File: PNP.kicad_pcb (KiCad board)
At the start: 4 copper layers, 98.3 x 100 mm, 41 parts, among them J1 Conn_01x04_Socket, J10 Screw_Terminal_01x02, J2 Conn_01x04_Socket, J3 Conn_01x04_Socket, J4 Conn_01x06_Socket, J5 Conn_01x04_Socket, J6 Conn_01x04_Socket, J7 Conn_01x04_Socket, J8 Screw_Terminal_01x02, J9 Screw_Terminal_01x02, Q1 IRLZ44N, Q3 IRLZ44N, U1 ESP32-S3-DevKitC, U10 Right Joystick, U6 Left Joystick

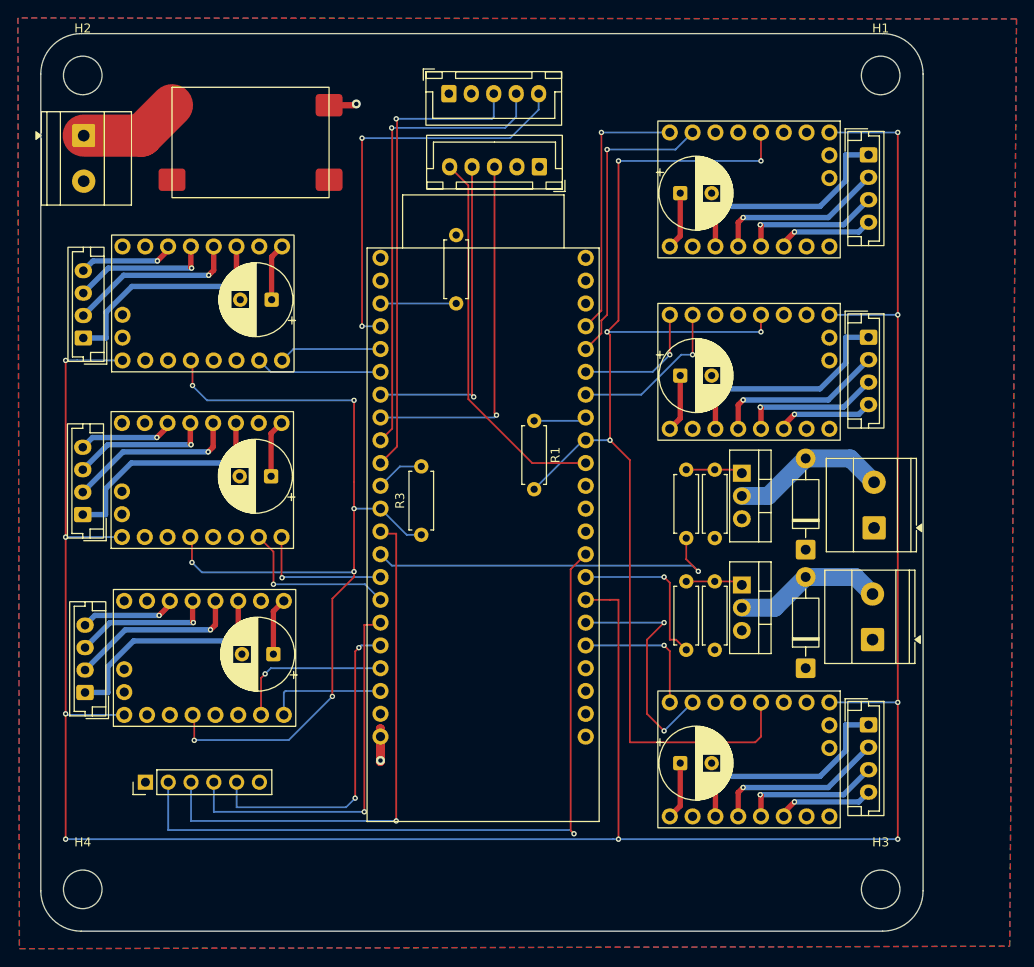
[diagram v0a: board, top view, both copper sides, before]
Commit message: Swap J4 to 2x06 header, drop KY-023 joysticks, rework TMC2209 daughterboard layout; add V0.2.0/V0.2.1 fab outputs
- PNP: J4 Conn_01x06 -> Conn_02x06 (PinHeader_2x06), removed Left/Right Joystick (U6/U10) from schematic and PCB, PCB re-routed (370 -> 366 segments area, vias 70 -> 58, zones 2 -> 1), ESP32-S3-DevKitC and MP1584EN footprints moved to Footprints lib, mask-to-copper clearance 0.005 mm
- TMC2209 daughterboard: PCB re-annotated/re-laid out (C5->C2, J6->J2, U8->U4, R7 removed)
- production/: PNP_V0.2.0 and V0.2.1 JLCPCB zips, BOM/CPL, netlist.ipc; fabrication-toolkit options
- code/: PlatformIO .gitignore and VS Code extension recommendations
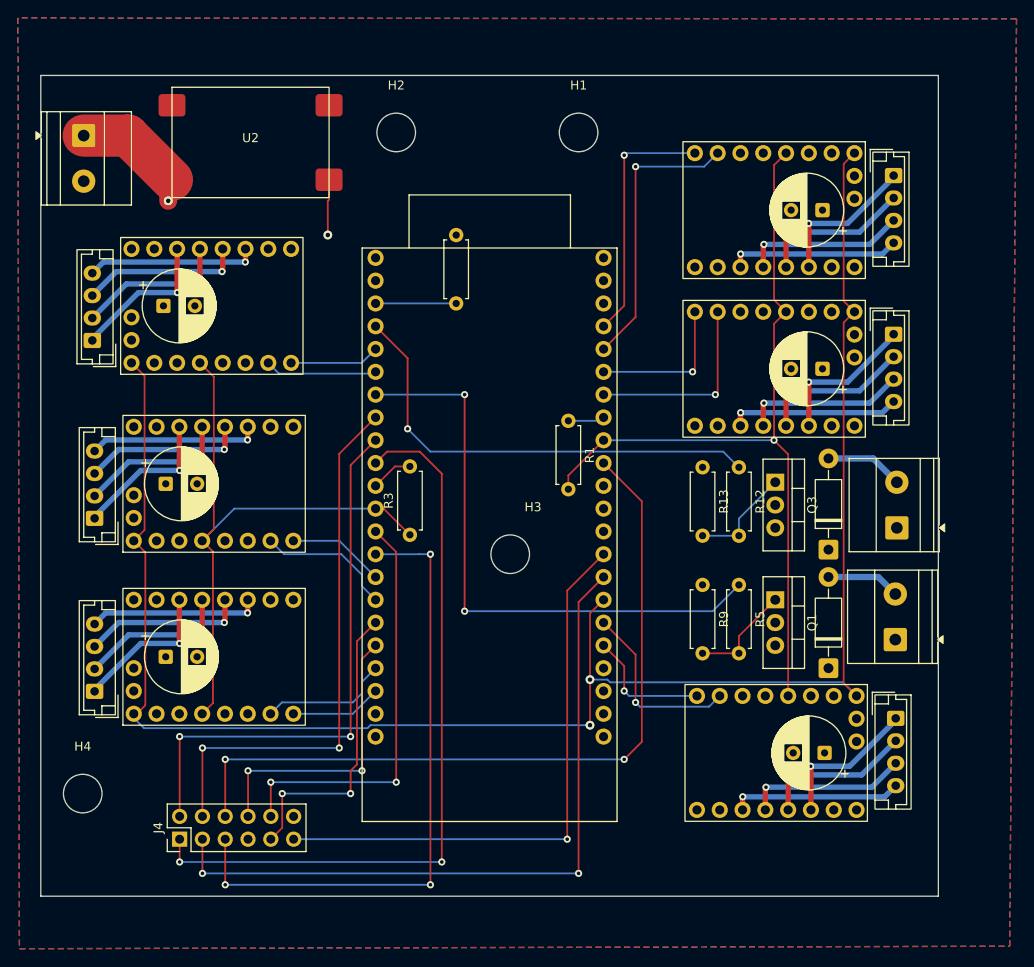
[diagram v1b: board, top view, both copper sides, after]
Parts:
- removed U10: Right Joystick, Connector_JST:JST_XH_B5B-XH-A_1x05_P2.50mm_Vertical
- removed U6: Left Joystick, Connector_JST:JST_XH_B5B-XH-A_1x05_P2.50mm_Vertical
- J4: footprint Connector_PinHeader_2.54mm:PinHeader_1x06_P2.54mm_Vertical -> Connector_PinHeader_2.54mm:PinHeader_2x06_P2.54mm_Vertical
- U1: footprint Espressif:ESP32-S3-DevKitC -> Footprints:ESP32-S3-DevKitC
- U2: footprint PNP:Mini MP1584EN Buck Converter Module -> Footprints:Mini MP1584EN Buck Converter Module
- moved H3 55.7 mm to (180.3, 95.2)
- moved H2 35.5 mm to (167.6, 48.3)
- moved H1 34.2 mm to (188.0, 48.3)
- moved C3 16.1 mm to (215.4, 117.4), turned to 180 degrees
- moved C2 16.0 mm to (215.1, 56.9), turned to 180 degrees
- moved C5 15.9 mm to (215.1, 74.6), turned to 180 degrees
- moved C6 12.1 mm to (141.7, 67.6), turned to 0 degrees
- moved C1 12.0 mm to (142.0, 106.7), turned to 0 degrees
- moved C4 11.8 mm to (142.0, 87.4), turned to 0 degrees
- moved H4 10.7 mm to (132.7, 121.9)
- moved R12 9.83 mm to (205.8, 85.6), turned to -90 degrees
- moved R5 9.31 mm to (205.8, 98.7), turned to -90 degrees
- moved R13 8.00 mm to (201.8, 85.6), turned to -90 degrees
- moved J4 7.41 mm to (143.5, 127.0)
- moved R9 7.36 mm to (201.8, 98.7), turned to -90 degrees
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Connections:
- J4 pad 1: +3.3V -> /GPIO17/ADC2_CH6
- J4 pad 2: /GPIO0 -> /GPIO16/ADC2_CH5/32K_N
- J4 pad 3: /GPIO3/ADC1_CH2 -> /GPIO45
- J4 pad 4: /GPIO11/ADC2_CH0 -> /GPIO15/ADC2_CH4/32K_P
- J4 pad 5: /GPIO12/ADC2_CH1 -> /GPIO46
- J4 pad 6: GND -> /GPIO38
- R12 pad 1: /GPIO46 -> /GPIO4/ADC1_CH3
- R5 pad 1: /GPIO45 -> /GPIO7/ADC1_CH6
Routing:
- net +3.3V: track 5.26 -> 256.1 mm
- net /GPIO48: track 297.2 -> 200.8 mm, vias 9 -> 2
- net /GPIO45: track 18.3 -> 79.9 mm, vias 1 -> 2
- net /GPIO39/MTCK: track 134.6 -> 89.9 mm, vias 5 -> 1
- net /GPIO38: track 42.8 -> 86.4 mm, vias 0 -> 2
- net /GPIO18/ADC2_CH7: track 106.5 -> 68.1 mm, vias 7 -> 0
- net /GPIO17/ADC2_CH6: track 52.7 -> 83.9 mm, vias 1 -> 2
- net /GPIO46: track 40.5 -> 70.9 mm, vias 1 -> 3
- net /GPIO7/ADC1_CH6: track 36.2 -> 65.8 mm, vias 1 -> 2
- net /GPIO15/ADC2_CH4/32K_P: track 40.8 -> 61.4 mm, vias 1 -> 2
- net +24V: track 300.8 -> 280.8 mm, vias 0 -> 1
- net /GPIO0: track 82.7 -> 63.9 mm
- net /GPIO3/ADC1_CH2: track 61.0 -> 46.7 mm, vias 1 -> 2
- net /GPIO16/ADC2_CH5/32K_N: track 52.3 -> 62.1 mm, vias 1 -> 2
- net /GPIO11/ADC2_CH0: track 42.8 -> 33.4 mm, vias 1 -> 2
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- added copper zone on In2.Cu, net GND
- removed copper zone on In2.Cu, net +3.3V
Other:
- board size 98.3 x 100 mm -> 100 x 91.4 mm
